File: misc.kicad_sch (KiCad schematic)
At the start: 25 parts, among them J7 Conn_ARM_JTAG_SWD_10, SW2 SW_DIP_x02, U1 MIMX8MM6DVTLZAA, Y3 24Mhz

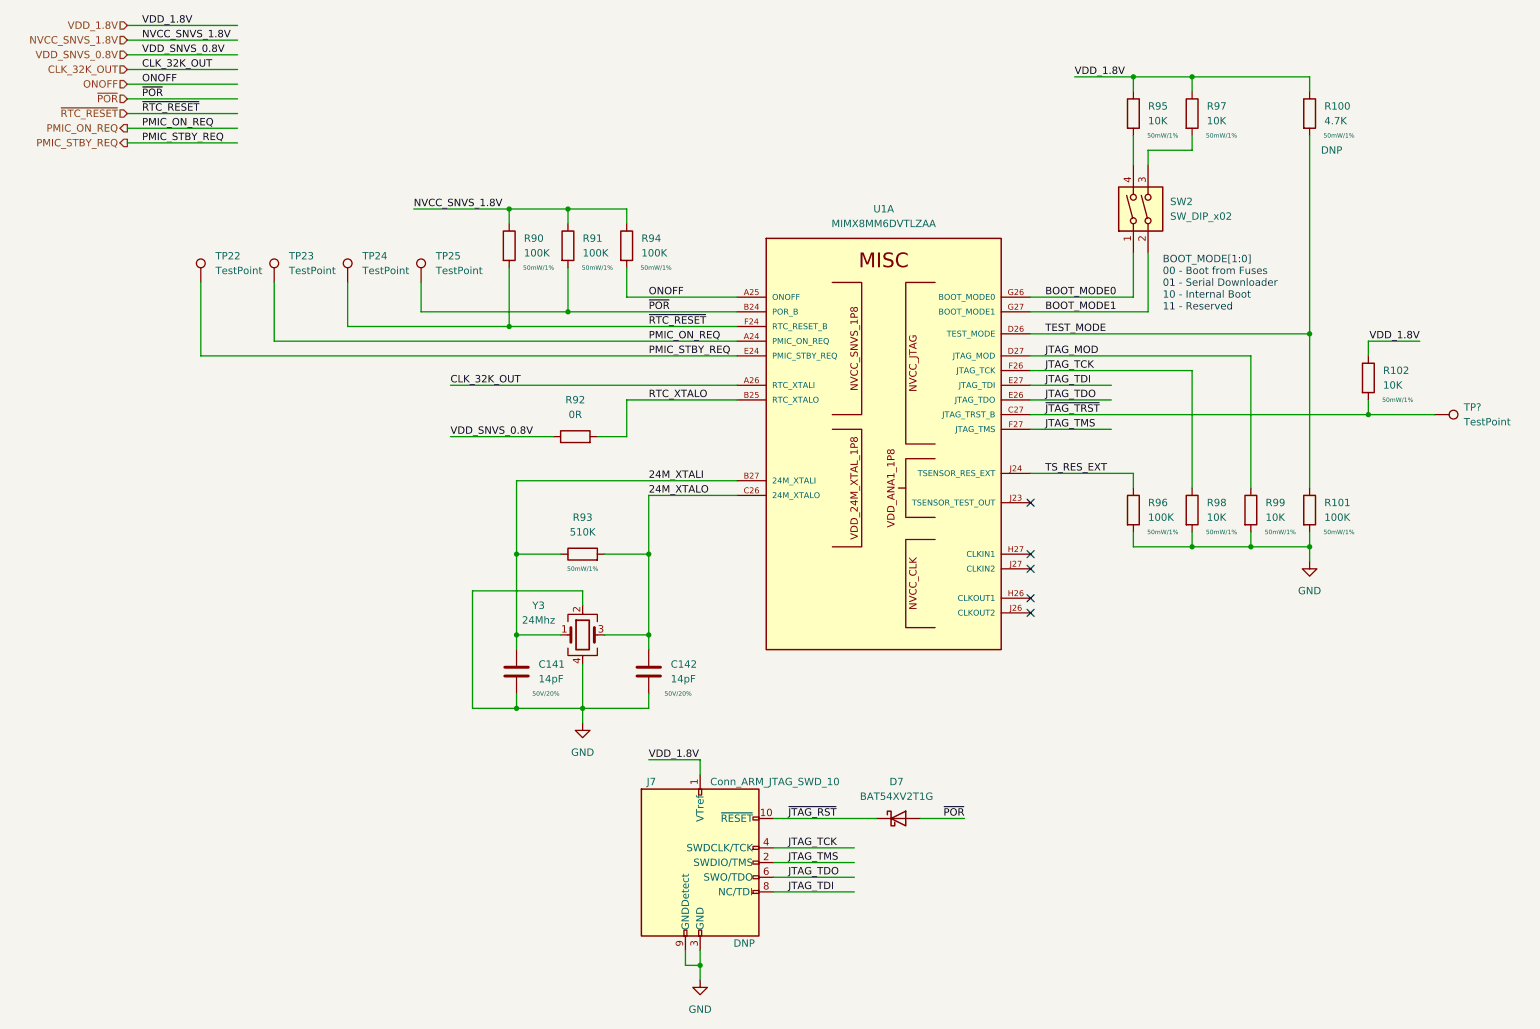
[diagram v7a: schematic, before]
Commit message: misc cleanup, change from usb mux to dual uart
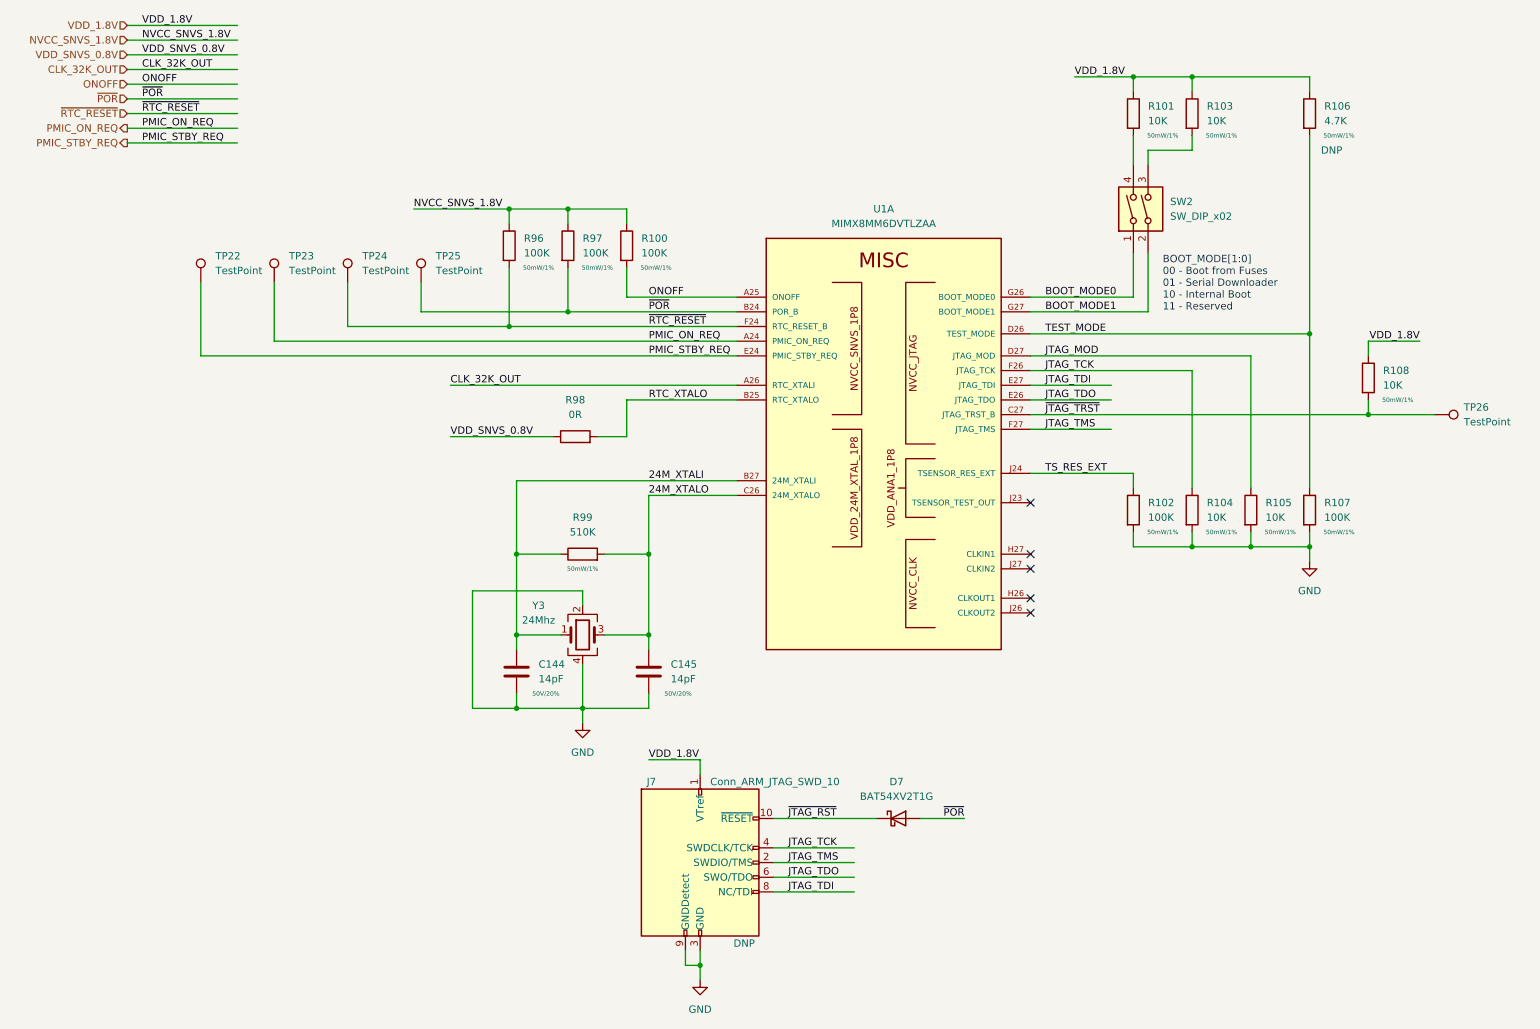
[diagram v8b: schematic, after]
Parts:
- TP22, TP23, TP24, TP25: now left out of the parts list
- TP26: renamed from TP?; now left out of the parts list
- renumbered C141 to C144, C142 to C145, R94 to R100, R95 to R101, R96 to R102, R97 to R103, R98 to R104, R99 to R105, R100 to R106, R101 to R107, R102 to R108, R90 to R96, R91 to R97, R92 to R98, R93 to R99
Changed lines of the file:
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@@
   (symbol (lib_id "Device:C") (at 97.79 132.08 0) (unit 1)
     (in_bom yes) (on_board yes)
-    (property "Reference" "C141" (id 0) (at 101.6 130.8099 0)
+    (property "Reference" "C144" (id 0) (at 101.6 130.8099 0)
       (effects (font (size 1.27 1.27)) (justify left))
     )
@@
   (symbol (lib_id "Device:R") (at 224.79 104.14 0) (unit 1)
     (in_bom yes) (on_board yes)
-    (property "Reference" "R99" (id 0) (at 227.33 102.8699 0)
+    (property "Reference" "R105" (id 0) (at 227.33 102.8699 0)
       (effects (font (size 1.27 1.27)) (justify left))
     )
@@
   (symbol (lib_id "power:GND") (at 129.54 185.42 0) (unit 1)
     (in_bom yes) (on_board yes) (fields_autoplaced)
-    (property "Reference" "#PWR0135" (id 0) (at 129.54 191.77 0)
+    (property "Reference" "#PWR0139" (id 0) (at 129.54 191.77 0)
       (effects (font (size 1.27 1.27)) hide)
     )
@@
   )
   (symbol (lib_id "Connector:TestPoint") (at 256.54 87.63 270) (unit 1)
-    (in_bom yes) (on_board yes) (fields_autoplaced)
-    (property "Reference" "TP?" (id 0) (at 261.62 86.3599 90)
+    (in_bom no) (on_board yes) (fields_autoplaced)
+    (property "Reference" "TP26" (id 0) (at 261.62 86.3599 90)
       (effects (font (size 1.27 1.27)) (justify left))
     )
@@
   (symbol (lib_id "Device:R") (at 214.63 35.56 0) (unit 1)
     (in_bom yes) (on_board yes)
-    (property "Reference" "R97" (id 0) (at 217.17 34.2899 0)
+    (property "Reference" "R103" (id 0) (at 217.17 34.2899 0)
       (effects (font (size 1.27 1.27)) (justify left))
     )
@@
   (symbol (lib_id "Device:R") (at 234.95 35.56 0) (unit 1)
     (in_bom yes) (on_board yes)
-    (property "Reference" "R100" (id 0) (at 237.49 34.2899 0)
+    (property "Reference" "R106" (id 0) (at 237.49 34.2899 0)
       (effects (font (size 1.27 1.27)) (justify left))
     )
@@
   )
   (symbol (lib_id "Connector:TestPoint") (at 81.28 64.77 0) (unit 1)
-    (in_bom yes) (on_board yes) (fields_autoplaced)
+    (in_bom no) (on_board yes) (fields_autoplaced)
     (property "Reference" "TP25" (id 0) (at 83.82 60.1979 0)
       (effects (font (size 1.27 1.27)) (justify left))
@@
   (symbol (lib_id "Device:R") (at 204.47 35.56 0) (unit 1)
     (in_bom yes) (on_board yes)
-    (property "Reference" "R95" (id 0) (at 207.01 34.2899 0)
+    (property "Reference" "R101" (id 0) (at 207.01 34.2899 0)
       (effects (font (size 1.27 1.27)) (justify left))
     )
@@
   (symbol (lib_id "Device:R") (at 96.52 58.42 0) (unit 1)
     (in_bom yes) (on_board yes)
-    (property "Reference" "R90" (id 0) (at 99.06 57.1499 0)
+    (property "Reference" "R96" (id 0) (at 99.06 57.1499 0)
       (effects (font (size 1.27 1.27)) (justify left))
     )
@@
   (symbol (lib_id "Device:R") (at 109.22 111.76 90) (unit 1)
     (in_bom yes) (on_board yes)
-    (property "Reference" "R93" (id 0) (at 109.22 105.41 90))
+    (property "Reference" "R99" (id 0) (at 109.22 105.41 90))
     (property "Value" "510K" (id 1) (at 109.22 107.95 90))
     (property "Footprint" "qsbc:R_0402_1005Metric" (id 2) (at 109.22 113.538 90)
@@
   (symbol (lib_id "power:GND") (at 109.22 140.97 0) (unit 1)
     (in_bom yes) (on_board yes) (fields_autoplaced)
-    (property "Reference" "#PWR0134" (id 0) (at 109.22 147.32 0)
+    (property "Reference" "#PWR0138" (id 0) (at 109.22 147.32 0)
       (effects (font (size 1.27 1.27)) hide)
     )
@@
   )
   (symbol (lib_id "Connector:TestPoint") (at 68.58 64.77 0) (unit 1)
-    (in_bom yes) (on_board yes) (fields_autoplaced)
+    (in_bom no) (on_board yes) (fields_autoplaced)
     (property "Reference" "TP24" (id 0) (at 71.12 60.1979 0)
       (effects (font (size 1.27 1.27)) (justify left))
@@
   (symbol (lib_id "Device:R") (at 234.95 104.14 0) (unit 1)
     (in_bom yes) (on_board yes)
-    (property "Reference" "R101" (id 0) (at 237.49 102.8699 0)
+    (property "Reference" "R107" (id 0) (at 237.49 102.8699 0)
       (effects (font (size 1.27 1.27)) (justify left))
     )
@@
   (symbol (lib_id "Device:R") (at 214.63 104.14 0) (unit 1)
     (in_bom yes) (on_board yes)
-    (property "Reference" "R98" (id 0) (at 217.17 102.8699 0)
+    (property "Reference" "R104" (id 0) (at 217.17 102.8699 0)
       (effects (font (size 1.27 1.27)) (justify left))
     )
@@
   (symbol (lib_id "Device:R") (at 116.84 58.42 0) (unit 1)
     (in_bom yes) (on_board yes)
-    (property "Reference" "R94" (id 0) (at 119.38 57.1499 0)
+    (property "Reference" "R100" (id 0) (at 119.38 57.1499 0)
       (effects (font (size 1.27 1.27)) (justify left))
     )
@@
   (symbol (lib_id "power:GND") (at 234.95 113.03 0) (unit 1)
     (in_bom yes) (on_board yes) (fields_autoplaced)
-    (property "Reference" "#PWR0136" (id 0) (at 234.95 119.38 0)
+    (property "Reference" "#PWR0140" (id 0) (at 234.95 119.38 0)
       (effects (font (size 1.27 1.27)) hide)
     )
@@
   (symbol (lib_id "Device:R") (at 204.47 104.14 0) (unit 1)
     (in_bom yes) (on_board yes)
-    (property "Reference" "R96" (id 0) (at 207.01 102.8699 0)
+    (property "Reference" "R102" (id 0) (at 207.01 102.8699 0)
       (effects (font (size 1.27 1.27)) (justify left))
     )
@@
   (symbol (lib_id "Device:C") (at 120.65 132.08 0) (unit 1)
     (in_bom yes) (on_board yes)
-    (property "Reference" "C142" (id 0) (at 124.46 130.8099 0)
+    (property "Reference" "C145" (id 0) (at 124.46 130.8099 0)
       (effects (font (size 1.27 1.27)) (justify left))
     )
@@
   (symbol (lib_id "Device:R") (at 245.11 81.28 0) (unit 1)
     (in_bom yes) (on_board yes)
-    (property "Reference" "R102" (id 0) (at 247.65 80.0099 0)
+    (property "Reference" "R108" (id 0) (at 247.65 80.0099 0)
       (effects (font (size 1.27 1.27)) (justify left))
     )
@@
   )
   (symbol (lib_id "Connector:TestPoint") (at 43.18 64.77 0) (unit 1)
-    (in_bom yes) (on_board yes) (fields_autoplaced)
+    (in_bom no) (on_board yes) (fields_autoplaced)
     (property "Reference" "TP22" (id 0) (at 45.72 60.1979 0)
       (effects (font (size 1.27 1.27)) (justify left))
@@
   (symbol (lib_id "Device:R") (at 106.68 58.42 0) (unit 1)
     (in_bom yes) (on_board yes)
-    (property "Reference" "R91" (id 0) (at 109.22 57.1499 0)
+    (property "Reference" "R97" (id 0) (at 109.22 57.1499 0)
       (effects (font (size 1.27 1.27)) (justify left))
     )
@@
   (symbol (lib_id "Device:R") (at 107.95 91.44 90) (unit 1)
     (in_bom yes) (on_board yes) (fields_autoplaced)
-    (property "Reference" "R92" (id 0) (at 107.95 85.09 90))
+    (property "Reference" "R98" (id 0) (at 107.95 85.09 90))
     (property "Value" "0R" (id 1) (at 107.95 87.63 90))
     (property "Footprint" "qsbc:R_0402_1005Metric" (id 2) (at 107.95 93.218 90)
@@
   )
   (symbol (lib_id "Connector:TestPoint") (at 55.88 64.77 0) (unit 1)
-    (in_bom yes) (on_board yes) (fields_autoplaced)
+    (in_bom no) (on_board yes) (fields_autoplaced)
     (property "Reference" "TP23" (id 0) (at 58.42 60.1979 0)
       (effects (font (size 1.27 1.27)) (justify left))
